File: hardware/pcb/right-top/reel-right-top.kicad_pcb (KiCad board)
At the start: 2 copper layers, 134.6 x 86.9 mm, 46 parts, among them J1 Conn_01x02, SW1 SW_Push, SW10 SW_Push, SW11 SW_Push, SW12 SW_Push, SW13 SW_Push, SW14 SW_Push, SW15 SW_Push, SW16 SW_Push, SW17 SW_Push, SW18 SW_Push, SW19 SW_Push, SW2 SW_Push, SW22 SW_SPDT, SW3 SW_Push, SW4 SW_Push, SW5 SW_Push, SW6 SW_Push, SW7 SW_Push, SW8 SW_Push, SW9 SW_Push

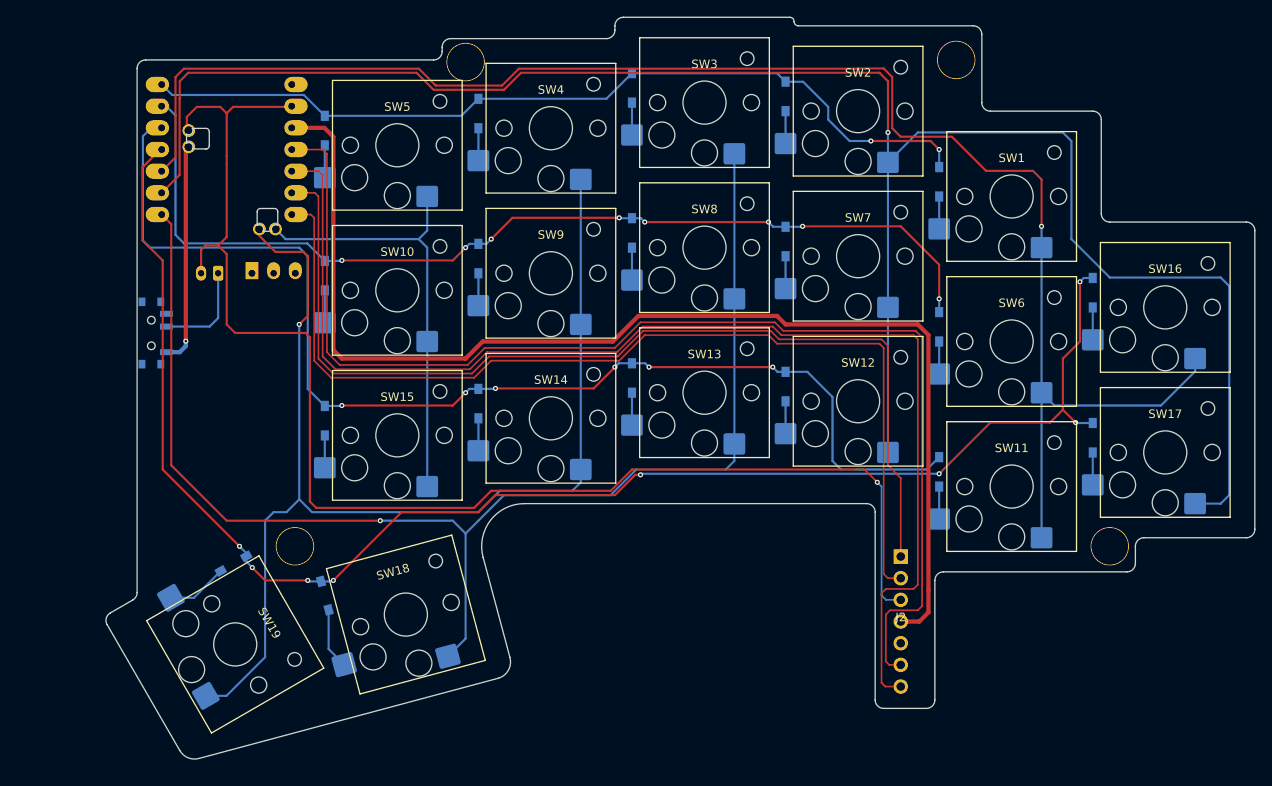
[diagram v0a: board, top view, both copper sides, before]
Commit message: Update PCB layouts and mechanical assets
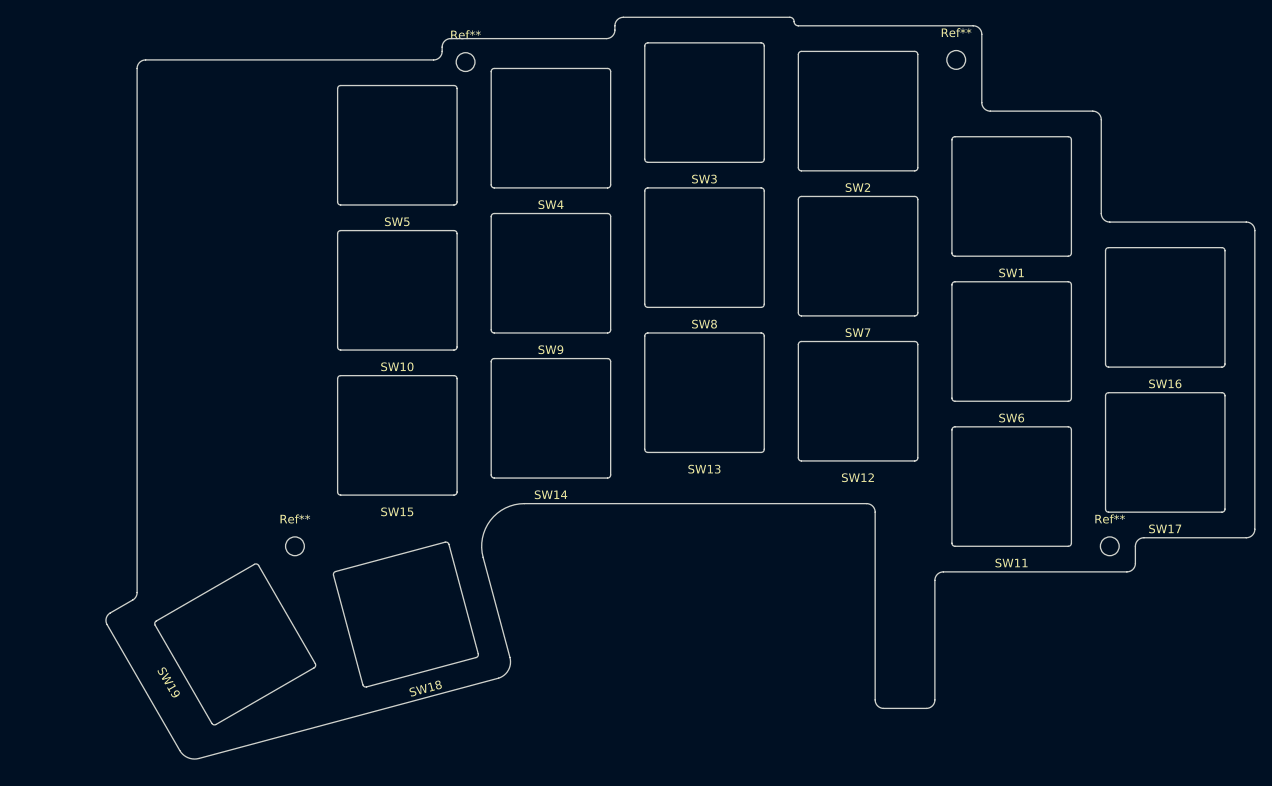
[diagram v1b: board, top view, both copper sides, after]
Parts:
- removed D1, D10, D11, D12, D13, D14, D15, D16, D17, D18, D19, D2, D3, D4, D5, D6, D7, D8, D9: D, reel:Diode_SMD
- removed J1: Conn_01x02, Connector_JST:JST_PH_S2B-PH-K_1x02_P2.00mm_Horizontal
- removed J2: ~, reel:pmw3610_connector
- removed SW22: SW_SPDT, Button_Switch_SMD:SW_SPDT_PCM12
- removed U1: ~, reel:XIAO_nRF52840_wBAT_wNFC_1
- Ref** (x4): footprint reel:m2_Spacer_Hole -> MountingHole:MountingHole_2.2mm_M2
- SW1, SW10, SW11, SW12, SW13, SW14, SW15, SW16, SW17, SW18, SW19, SW2, SW3, SW4, SW5, SW6, SW7, SW8, SW9: footprint reel:SW_Hotswap_Kailh_Choc_V1V2_1.00u -> reel:choc_plate
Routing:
- net Col1: track 227.5 -> 0.00 mm, vias 1 -> 0
- net Col0: track 187.9 -> 0.00 mm, vias 1 -> 0
- net Row3: track 181.1 -> 0.00 mm, vias 8 -> 0
- net GND: track 160.2 -> 0.00 mm, vias 1 -> 0
- net Col2: track 153.9 -> 0.00 mm, vias 1 -> 0
- net MOTION: track 144.5 -> 0.00 mm
- net SDIO: track 144.3 -> 0.00 mm
- net 3.3V: track 139.7 -> 0.00 mm
- net Row2: track 137.5 -> 0.00 mm, vias 6 -> 0
- net Col3: track 136.1 -> 0.00 mm, vias 1 -> 0
- net nCS: track 118.5 -> 0.00 mm
- net SCLK: track 117.5 -> 0.00 mm
- net Row1: track 116.8 -> 0.00 mm, vias 8 -> 0
- net Row0: track 101.4 -> 0.00 mm, vias 2 -> 0
- net Col4: track 51.8 -> 0.00 mm
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
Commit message: Update ReeL hardware and fabrication assets
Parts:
- added Ref**: Val**, MountingHole:MountingHole_2.2mm_M2, F.Cu at (137.5, 107.5)
- moved Ref** 10.0 mm to (58.0, 107.5)
- moved SW18 10.0 mm to (71.0, 115.5)
- moved SW19 10.0 mm to (51.0, 119.0)
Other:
- board size 134.6 x 86.9 mm -> 143 x 86.6 mm
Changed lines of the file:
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@@
 		(filling no)
 		(pcbplotparams
-			(layerselection 0x00000000_00000000_55555555_5755f5ff)
+			(layerselection 0x00000000_00000000_55555555_57555550)
 			(plot_on_all_layers_selection 0x00000000_00000000_00000000_00000000)
 			(disableapertmacros no)
@@
 			(pdf_metadata yes)
 			(pdf_single_document no)
-			(dxfpolygonmode yes)
-			(dxfimperialunits yes)
-			(dxfusepcbnewfont yes)
+			(dxfpolygonmode no)
+			(dxfimperialunits no)
+			(dxfusepcbnewfont no)
 			(psnegative no)
 			(psa4output no)
@@
 			(crossoutdnponfab yes)
 			(subtractmaskfromsilk no)
-			(outputformat 1)
+			(outputformat 3)
 			(mirror no)
-			(drillshape 1)
+			(drillshape 0)
 			(scaleselection 1)
 			(outputdirectory "")
@@
 		)
 	)
+	(footprint "MountingHole:MountingHole_2.2mm_M2"
+		(layer "F.Cu")
+		(at 137.5 107.5)
+		(descr "Mounting Hole 2.2mm, M2, no annular, generated by kicad-footprint-generator mountinghole.py")
+		(tags "mountinghole M2")
+		(property "Reference" "Ref**"
+			(at 0 -3.15 0)
+			(layer "F.SilkS")
+			(effects
+				(font
+					(size 1 1)
+					(thickness 0.15)
+				)
+			)
+		)
+		(property "Value" "Val**"
+			(at 0 3.15 0)
+			(layer "F.Fab")
+			(effects
+				(font
+					(size 1 1)
+					(thickness 0.15)
+				)
+			)
+		)
+		(property "Datasheet" ""
+			(at 0 0 0)
+			(layer "F.Fab")
+			(hide yes)
+			(effects
+				(font
+					(size 1.27 1.27)
+				)
+			)
+		)
+		(property "Description" ""
+			(at 0 0 0)
+			(layer "F.Fab")
+			(hide yes)
+			(effects
+				(font
+					(size 1.27 1.27)
+				)
+			)
+		)
+		(property "KiLib_Generator" "mounting_hardware/mounting_hole"
+			(at 0 0 0)
+			(layer "F.SilkS")
+			(hide yes)
+			(effects
+				(font
+					(size 1 1)
+					(thickness 0.15)
+				)
+			)
+		)
+		(attr exclude_from_pos_files exclude_from_bom)
+		(duplicate_pad_numbers_are_jumpers no)
+		(fp_circle
+			(center 0 0)
+			(end 2.2 0)
+			(stroke
+				(width 0.15)
+				(type solid)
+			)
+			(fill no)
+			(layer "Cmts.User")
+		)
+		(fp_circle
+			(center 0 0)
+			(end 2.45 0)
+			(stroke
+				(width 0.05)
+				(type solid)
+			)
+			(fill no)
+			(layer "F.CrtYd")
+		)
+		(fp_text user "${REFERENCE}"
+			(at 0 0 0)
+			(layer "F.Fab")
+			(effects
+				(font
+					(size 1 1)
+					(thickness 0.15)
+				)
+			)
+		)
+		(pad "" np_thru_hole circle
+			(at 0 0)
+			(size 2.2 2.2)
+			(drill 2.2)
+			(layers "*.Cu" "*.Mask")
+		)
+		(embedded_fonts no)
+	)
 	(footprint "reel:choc_plate"
 		(layer "F.Cu")
@@
 	(footprint "reel:choc_plate"
 		(layer "F.Cu")
-		(at 81 115.5 -165)
+		(at 71 115.5 -165)
 		(descr "Kailh Choc V1V2 CPG1350/CPG1353 hotswap")
 		(property "Reference" "SW18"
@@
 	(footprint "reel:choc_plate"
 		(layer "F.Cu")
-		(at 61 119 120)
+		(at 51 119 120)
 		(descr "Kailh Choc V1V2 CPG1350/CPG1353 hotswap")
 		(property "Reference" "SW19"
@@
 	(footprint "MountingHole:MountingHole_2.2mm_M2"
 		(layer "F.Cu")
-		(at 68 107.5)
+		(at 58 107.5)
 		(descr "Mounting Hole 2.2mm, M2, no annular, generated by kicad-footprint-generator mountinghole.py")
 		(tags "mountinghole M2")
@@
 	)
 	(gr_arc
-		(start 45.986856 116.683017)
-		(mid 45.886954 115.924197)
-		(end 46.35288 115.31699)
+		(start 37.589746 115.772758)
+		(mid 37.489877 115.013958)
+		(end 37.955771 114.406733)
 		(stroke
 			(width 0.05)
@@
 	)
 	(gr_line
-		(start 45.986856 116.683017)
-		(end 54.503472 131.434154)
+		(start 37.589746 115.772758)
+		(end 46.722209 131.590648)
 		(stroke
 			(width 0.05)
@@
 	)
 	(gr_line
-		(start 46.35288 115.31699)
-		(end 49 113.788675)
+		(start 37.955771 114.406733)
+		(end 47 109.185045)
 		(stroke
 			(width 0.05)
@@
 		(layer "Edge.Cuts")
 	)
+	(gr_arc
+		(start 47.847054 132.056574)
+		(mid 47.205532 132.014546)
+		(end 46.722209 131.590648)
+		(stroke
+			(width 0.05)
+			(type default)
+		)
+		(layer "Edge.Cuts")
+	)
 	(gr_line
 		(start 49.5 51.5)
-		(end 49.5 112.92265)
+		(end 49.5 104.854918)
 		(stroke
 			(width 0.05)
@@
 	)
 	(gr_arc
-		(start 49.5 112.92265)
-		(mid 49.366025 113.42265)
-		(end 49 113.788675)
+		(start 49.5 104.854918)
+		(mid 48.83012 107.354912)
+		(end 47 109.185045)
 		(stroke
 			(width 0.05)
@@
 	)
 	(gr_arc
-		(start 56.753158 132.366002)
-		(mid 55.470155 132.28191)
-		(end 54.503472 131.434154)
+		(start 80.609457 110.794095)
+		(mid 81.47232 106.456193)
+		(end 85.439086 104.5)
+		(stroke
+			(width 0.05)
+			(type default)
+		)
+		(layer "Edge.Cuts")
+	)
+	(gr_line
+		(start 82.764485 122.700476)
+		(end 47.847054 132.056574)
+		(stroke
+			(width 0.05)
+			(type solid)
+		)
+		(layer "Edge.Cuts")
+	)
+	(gr_line
+		(start 83.471592 121.475731)
+		(end 80.609457 110.794095)
+		(stroke
+			(width 0.05)
+			(type solid)
+		)
+		(layer "Edge.Cuts")
+	)
+	(gr_arc
+		(start 83.471592 121.475731)
+		(mid 83.371665 122.234514)
+		(end 82.764485 122.700476)
 		(stroke
 			(width 0.05)
@@
 	)
 	(gr_line
-		(start 90.052523 108.794095)
-		(end 93.19777 120.532314)
+		(start 89.5 104.5)
+		(end 85.439086 104.5)
 		(stroke
 			(width 0.05)
-			(type solid)
+			(type default)
 		)
 		(layer "Edge.Cuts")
 	)
 	(gr_arc
-		(start 90.052523 108.794095)
-		(mid 90.915386 104.456193)
-		(end 94.882152 102.5)
+		(start 90.5 103.5)
+		(mid 90.207107 104.207107)
+		(end 89.5 104.5)
 		(stroke
 			(width 0.05)
@@
 		(layer "Edge.Cuts")
 	)
-	(gr_line
-		(start 91.871403 122.956097)
-		(end 56.753158 132.366002)
+	(gr_arc
+		(start 90.5 103.5)
+		(mid 90.792893 102.792893)
+		(end 91.5 102.5)
 		(stroke
 			(width 0.05)
-			(type solid)
+			(type default)
 		)
 		(layer "Edge.Cuts")
 	)
-	(gr_arc
-		(start 93.19777 120.532314)
-		(mid 93.020424 122.010086)
-		(end 91.871403 122.956097)
+	(gr_line
+		(start 91.5 102.5)
+		(end 125 102.5)
 		(stroke
 			(width 0.05)
-			(type default)
+			(type solid)
 		)
 		(layer "Edge.Cuts")
@@
 	)
 	(gr_arc
-		(start 126 45.5)
-		(mid 126.353553 45.646447)
-		(end 126.5 46)
+		(start 125 102.5)
+		(mid 125.707107 102.792893)
+		(end 126 103.5)
 		(stroke
 			(width 0.05)
@@
 	)
 	(gr_arc
-		(start 127 46.5)
-		(mid 126.646447 46.353553)
+		(start 126 45.5)
+		(mid 126.353553 45.646447)
 		(end 126.5 46)
 		(stroke
@@
 	)
 	(gr_line
-		(start 127 46.5)
-		(end 147.5 46.5)
-		(stroke
-			(width 0.05)
-			(type default)
-		)
-		(layer "Edge.Cuts")
-	)
-	(gr_line
-		(start 135 102.5)
-		(end 94.882152 102.5)
+		(start 126 126)
+		(end 126 103.5)
 		(stroke
 			(width 0.05)
-			(type default)
+			(type solid)
 		)
 		(layer "Edge.Cuts")
 	)
 	(gr_arc
-		(start 135 102.5)
-		(mid 135.707107 102.792893)
-		(end 136 103.5)
+		(start 127 46.5)
+		(mid 126.646447 46.353553)
+		(end 126.5 46)
 		(stroke
 			(width 0.05)
@@
 	)
 	(gr_line
-		(start 136 125.5)
-		(end 136 103.5)
+		(start 127 46.5)
+		(end 147.5 46.5)
 		(stroke
 			(width 0.05)
-			(type solid)
+			(type default)
 		)
 		(layer "Edge.Cuts")
 	)
 	(gr_arc
-		(start 137 126.5)
-		(mid 136.292893 126.207107)
-		(end 136 125.5)
+		(start 127 127)
+		(mid 126.292893 126.707107)
+		(end 126 126)
 		(stroke
 			(width 0.05)
@@
 	)
 	(gr_line
-		(start 142 126.5)
-		(end 137 126.5)
+		(start 132 127)
+		(end 127 127)
 		(stroke
 			(width 0.05)
-			(type default)
+			(type solid)
 		)
 		(layer "Edge.Cuts")
 	)
 	(gr_line
-		(start 143 111.5)
-		(end 143 125.5)
-		(stroke
-			(width 0.05)
-			(type default)
-		)
-		(layer "Edge.Cuts")
-	)
-	(gr_arc
-		(start 143 111.5)
-		(mid 143.292893 110.792893)
-		(end 144 110.5)
+		(start 133 110.5)
+		(end 133 126)
 		(stroke
 			(width 0.05)
-			(type default)
+			(type solid)
 		)
 		(layer "Edge.Cuts")
 	)
 	(gr_arc
-		(start 143 125.5)
-		(mid 142.707107 126.207107)
-		(end 142 126.5)
+		(start 133 126)
+		(mid 132.707107 126.707107)
+		(end 132 127)
 		(stroke
 			(width 0.05)
@@
 	(gr_line
 		(start 165.5 110.5)
-		(end 144 110.5)
+		(end 133 110.5)
 		(stroke
 			(width 0.05)

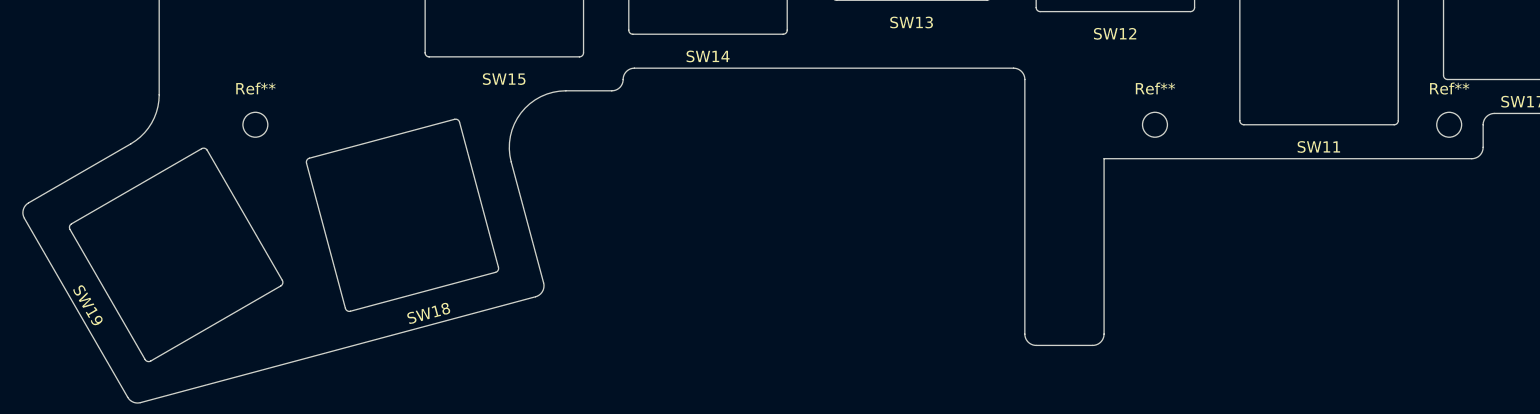
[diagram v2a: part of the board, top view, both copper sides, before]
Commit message: Update right plate PCB models
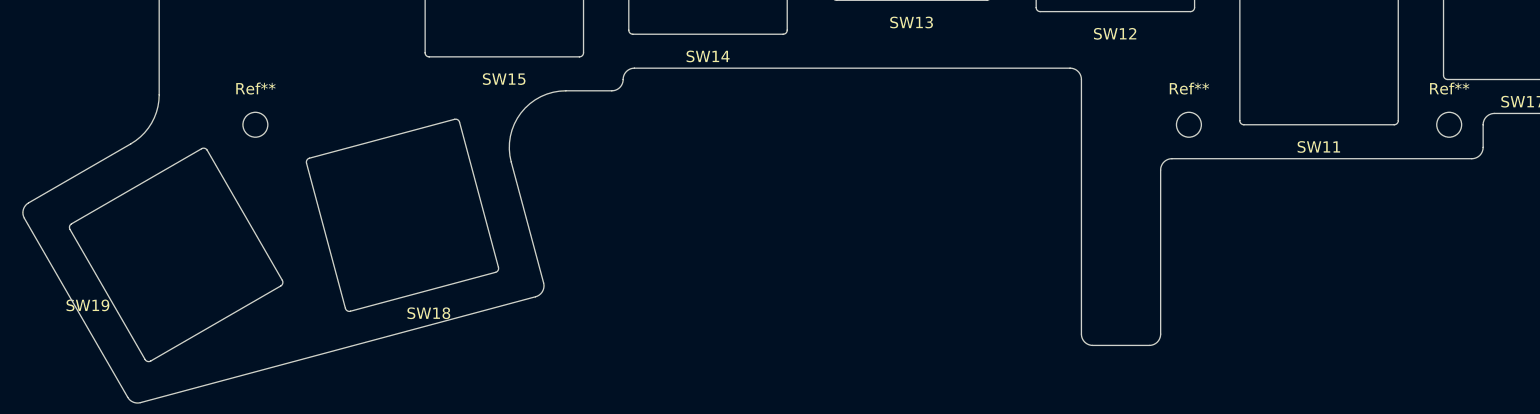
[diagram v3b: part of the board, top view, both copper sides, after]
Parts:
- Ref** (x5): value Val** -> MountingHole_2.2mm_M2
- SW1, SW10, SW11, SW12, SW13, SW14, SW15, SW16, SW17, SW18, SW19, SW2, SW3, SW4, SW5, SW6, SW7, SW8, SW9: value SW_Push -> choc_plate
- moved Ref** 3.00 mm to (140.5, 107.5)
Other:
- outline, holes or cut-outs redrawn
